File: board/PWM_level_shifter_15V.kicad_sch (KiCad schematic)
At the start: 0 parts

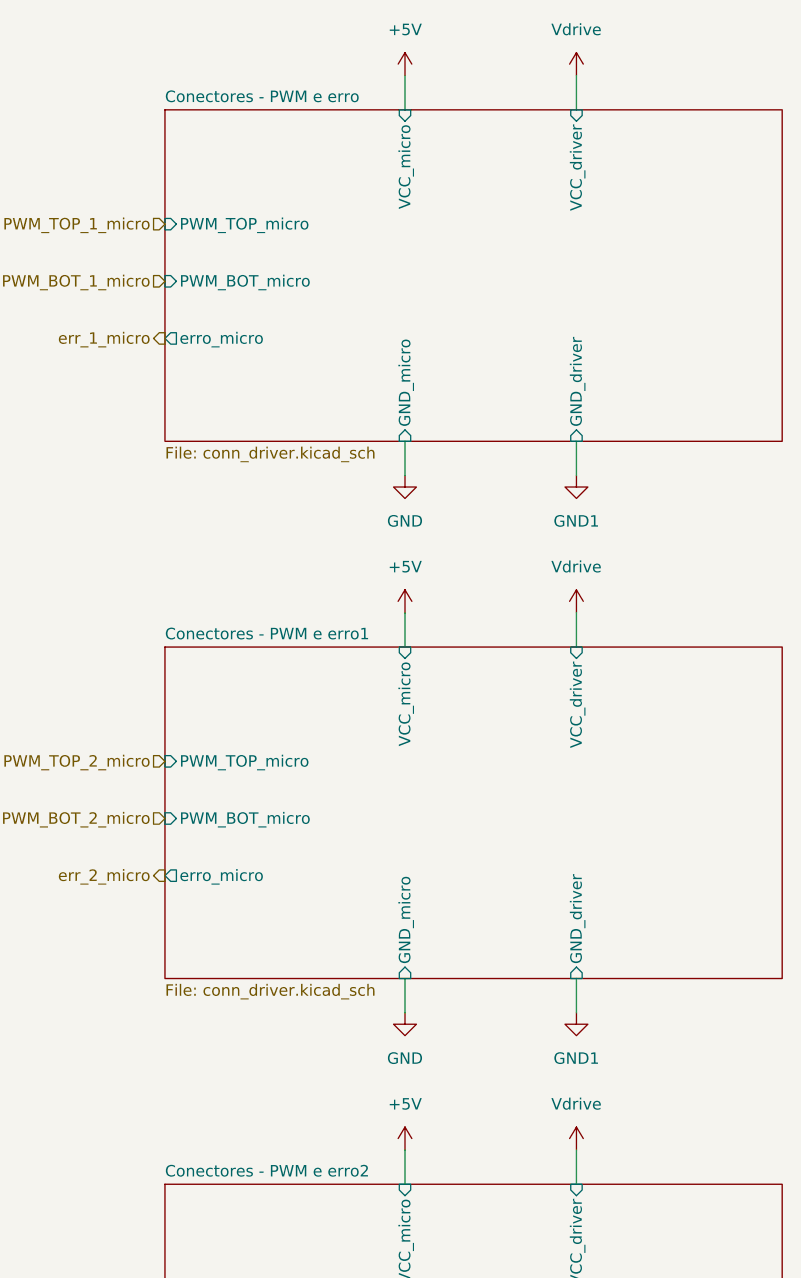
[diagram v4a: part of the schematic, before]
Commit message: Finalização da placa, trilhas, planos de terra e footprint TJA1050
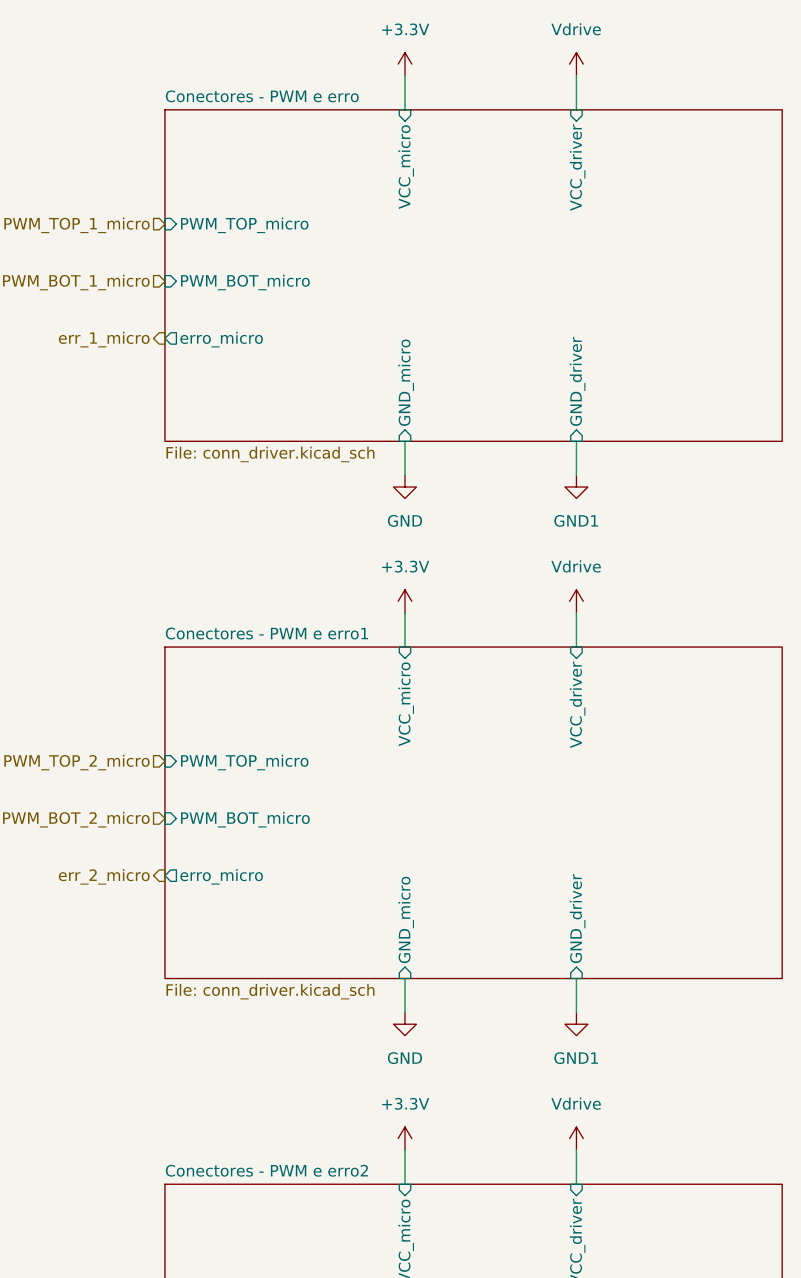
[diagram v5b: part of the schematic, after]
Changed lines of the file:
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@@
+	)
+	(symbol
+		(lib_id "power:+3.3V")
+		(at 68.58 82.55 0)
+		(unit 1)
+		(exclude_from_sim no)
+		(in_bom yes)
+		(on_board yes)
+		(dnp no)
+		(fields_autoplaced yes)
+		(property "Reference" "#PWR11"
+			(at 68.58 86.36 0)
+			(effects
+				(font
+					(size 1.27 1.27)
+				)
+				(hide yes)
+			)
+		)
+		(property "Value" "+3.3V"
+			(at 68.58 77.47 0)
+			(effects
+				(font
+					(size 1.27 1.27)
+				)
+			)
+		)
+		(property "Footprint" ""
+			(at 68.58 82.55 0)
+			(effects
+				(font
+					(size 1.27 1.27)
+				)
+				(hide yes)
+			)
+		)
+		(property "Datasheet" ""
+			(at 68.58 82.55 0)
+			(effects
+				(font
+					(size 1.27 1.27)
+				)
+				(hide yes)
+			)
+		)
+		(property "Description" "Power symbol creates a global label with name \"+3.3V\""
+			(at 68.58 82.55 0)
+			(effects
+				(font
+					(size 1.27 1.27)
+				)
+				(hide yes)
+			)
+		)
+		(pin "1"
+		)
+		(instances
+			(project "board"
+				(path "/d7be55ed-3561-4de6-aa99-76e883d44fb9/90c49c41-4e5e-4cb7-8d94-45cf3dbd4784"
+					(reference "#PWR11")
+					(unit 1)
+				)
+			)
+		)
 	)
 	(symbol
@@
 		(dnp no)
 		(fields_autoplaced yes)
-		(property "Reference" "#PWR20"
+		(property "Reference" "#PWR17"
 			(at 87.63 86.36 0)
 			(effects
@@
 			(project "board"
 				(path "/d7be55ed-3561-4de6-aa99-76e883d44fb9/90c49c41-4e5e-4cb7-8d94-45cf3dbd4784"
-					(reference "#PWR20")
+					(reference "#PWR17")
 					(unit 1)
 				)
@@
 		(on_board yes)
 		(dnp no)
-		(property "Reference" "#PWR17"
+		(property "Reference" "#PWR14"
 			(at 68.58 193.04 0)
 			(effects
@@
 			(project "board"
 				(path "/d7be55ed-3561-4de6-aa99-76e883d44fb9/90c49c41-4e5e-4cb7-8d94-45cf3dbd4784"
-					(reference "#PWR17")
-					(unit 1)
-				)
-			)
-		)
-	)
-	(symbol
-		(lib_id "power:+5V")
+					(reference "#PWR14")
+					(unit 1)
+				)
+			)
+		)
+	)
+	(symbol
+		(lib_id "power:+3.3V")
 		(at 68.58 22.86 0)
 		(unit 1)
@@
 		(dnp no)
 		(fields_autoplaced yes)
-		(property "Reference" "#PWR12"
+		(property "Reference" "#PWR9"
 			(at 68.58 26.67 0)
 			(effects
@@
 			)
 		)
-		(property "Value" "+5V"
+		(property "Value" "+3.3V"
 			(at 68.58 17.78 0)
 			(effects
@@
 			)
 		)
-		(property "Description" "Power symbol creates a global label with name \"+5V\""
+		(property "Description" "Power symbol creates a global label with name \"+3.3V\""
 			(at 68.58 22.86 0)
 			(effects
@@
 		)
 		(instances
-			(project "board"
-				(path "/d7be55ed-3561-4de6-aa99-76e883d44fb9/90c49c41-4e5e-4cb7-8d94-45cf3dbd4784"
-					(reference "#PWR12")
+			(project ""
+				(path "/d7be55ed-3561-4de6-aa99-76e883d44fb9/90c49c41-4e5e-4cb7-8d94-45cf3dbd4784"
+					(reference "#PWR9")
 					(unit 1)
 				)
@@
 		(dnp no)
 		(fields_autoplaced yes)
-		(property "Reference" "#PWR21"
+		(property "Reference" "#PWR18"
 			(at 87.63 133.35 0)
 			(effects
@@
 			(project "board"
 				(path "/d7be55ed-3561-4de6-aa99-76e883d44fb9/90c49c41-4e5e-4cb7-8d94-45cf3dbd4784"
-					(reference "#PWR21")
-					(unit 1)
-				)
-			)
-		)
-	)
-	(symbol
-		(lib_id "power:+5V")
+					(reference "#PWR18")
+					(unit 1)
+				)
+			)
+		)
+	)
+	(symbol
+		(lib_id "power:+3.3V")
 		(at 68.58 142.24 0)
 		(unit 1)
@@
 		(dnp no)
 		(fields_autoplaced yes)
-		(property "Reference" "#PWR16"
+		(property "Reference" "#PWR13"
 			(at 68.58 146.05 0)
 			(effects
@@
 			)
 		)
-		(property "Value" "+5V"
+		(property "Value" "+3.3V"
 			(at 68.58 137.16 0)
 			(effects
@@
 			)
 		)
-		(property "Description" "Power symbol creates a global label with name \"+5V\""
+		(property "Description" "Power symbol creates a global label with name \"+3.3V\""
 			(at 68.58 142.24 0)
 			(effects
@@
 			(project "board"
 				(path "/d7be55ed-3561-4de6-aa99-76e883d44fb9/90c49c41-4e5e-4cb7-8d94-45cf3dbd4784"
-					(reference "#PWR16")
+					(reference "#PWR13")
 					(unit 1)
 				)
@@
 		(dnp no)
 		(fields_autoplaced yes)
-		(property "Reference" "#PWR22"
+		(property "Reference" "#PWR19"
 			(at 87.63 146.05 0)
 			(effects
@@
 			(project "board"
 				(path "/d7be55ed-3561-4de6-aa99-76e883d44fb9/90c49c41-4e5e-4cb7-8d94-45cf3dbd4784"
-					(reference "#PWR22")
-					(unit 1)
-				)
-			)
-		)
-	)
-	(symbol
-		(lib_id "power:+5V")
-		(at 68.58 82.55 0)
-		(unit 1)
-		(exclude_from_sim no)
-		(in_bom yes)
-		(on_board yes)
-		(dnp no)
-		(fields_autoplaced yes)
-		(property "Reference" "#PWR14"
-			(at 68.58 86.36 0)
-			(effects
-				(font
-					(size 1.27 1.27)
-				)
-				(hide yes)
-			)
-		)
-		(property "Value" "+5V"
-			(at 68.58 77.47 0)
-			(effects
-				(font
-					(size 1.27 1.27)
-				)
-			)
-		)
-		(property "Footprint" ""
-			(at 68.58 82.55 0)
-			(effects
-				(font
-					(size 1.27 1.27)
-				)
-				(hide yes)
-			)
-		)
-		(property "Datasheet" ""
-			(at 68.58 82.55 0)
-			(effects
-				(font
-					(size 1.27 1.27)
-				)
-				(hide yes)
-			)
-		)
-		(property "Description" "Power symbol creates a global label with name \"+5V\""
-			(at 68.58 82.55 0)
-			(effects
-				(font
-					(size 1.27 1.27)
-				)
-				(hide yes)
-			)
-		)
-		(pin "1"
-		)
-		(instances
-			(project "board"
-				(path "/d7be55ed-3561-4de6-aa99-76e883d44fb9/90c49c41-4e5e-4cb7-8d94-45cf3dbd4784"
-					(reference "#PWR14")
+					(reference "#PWR19")
 					(unit 1)
 				)
@@
 		(on_board yes)
 		(dnp no)
-		(property "Reference" "#PWR13"
+		(property "Reference" "#PWR10"
 			(at 68.58 73.66 0)
 			(effects
@@
 			(project "board"
 				(path "/d7be55ed-3561-4de6-aa99-76e883d44fb9/90c49c41-4e5e-4cb7-8d94-45cf3dbd4784"
-					(reference "#PWR13")
+					(reference "#PWR10")
 					(unit 1)
 				)
@@
 		(dnp no)
 		(fields_autoplaced yes)
-		(property "Reference" "#PWR19"
+		(property "Reference" "#PWR16"
 			(at 87.63 73.66 0)
 			(effects
@@
 			(project "board"
 				(path "/d7be55ed-3561-4de6-aa99-76e883d44fb9/90c49c41-4e5e-4cb7-8d94-45cf3dbd4784"
-					(reference "#PWR19")
+					(reference "#PWR16")
 					(unit 1)
 				)
@@
 		(dnp no)
 		(fields_autoplaced yes)
-		(property "Reference" "#PWR23"
+		(property "Reference" "#PWR20"
 			(at 87.63 193.04 0)
 			(effects
@@
 			(project "board"
 				(path "/d7be55ed-3561-4de6-aa99-76e883d44fb9/90c49c41-4e5e-4cb7-8d94-45cf3dbd4784"
-					(reference "#PWR23")
+					(reference "#PWR20")
 					(unit 1)
 				)
@@
 		(on_board yes)
 		(dnp no)
-		(property "Reference" "#PWR15"
+		(property "Reference" "#PWR12"
 			(at 68.58 133.35 0)
 			(effects
@@
 			(project "board"
 				(path "/d7be55ed-3561-4de6-aa99-76e883d44fb9/90c49c41-4e5e-4cb7-8d94-45cf3dbd4784"
-					(reference "#PWR15")
+					(reference "#PWR12")
 					(unit 1)
 				)
@@
 		(dnp no)
 		(fields_autoplaced yes)
-		(property "Reference" "#PWR18"
+		(property "Reference" "#PWR15"
 			(at 87.63 26.67 0)
 			(effects
@@
 			(project "board"
 				(path "/d7be55ed-3561-4de6-aa99-76e883d44fb9/90c49c41-4e5e-4cb7-8d94-45cf3dbd4784"
-					(reference "#PWR18")
-					(unit 1)
-				)
+					(reference "#PWR15")
+					(unit 1)
+				)

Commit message: Criação da placa de alimentação
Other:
- company: (none) -> Escola Politécnica da Universidade de São Paulo
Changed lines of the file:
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@@
 	(generator_version "8.0")
 	(paper "A4")
+	(title_block
+		(date "2025-10-02")
+		(company "Escola Politécnica da Universidade de São Paulo")
+	)
 	(wire
 		(pts
@@
 			(project "board"
 				(path "/d7be55ed-3561-4de6-aa99-76e883d44fb9/90c49c41-4e5e-4cb7-8d94-45cf3dbd4784"
-					(page "20")
+					(page "5")
 				)
 			)
@@
 			(project "board"
 				(path "/d7be55ed-3561-4de6-aa99-76e883d44fb9/90c49c41-4e5e-4cb7-8d94-45cf3dbd4784"
-					(page "26")
+					(page "6")
 				)
 			)
@@
 			(project "board"
 				(path "/d7be55ed-3561-4de6-aa99-76e883d44fb9/90c49c41-4e5e-4cb7-8d94-45cf3dbd4784"
-					(page "16")
-				)
-			)
+					(page "4")
+				)
+			)
